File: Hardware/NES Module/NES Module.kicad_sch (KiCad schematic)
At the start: 3 parts, among them J1 Conn_01x31, J2 Conn_01x31, J3 Conn_02x36_Top_Bottom

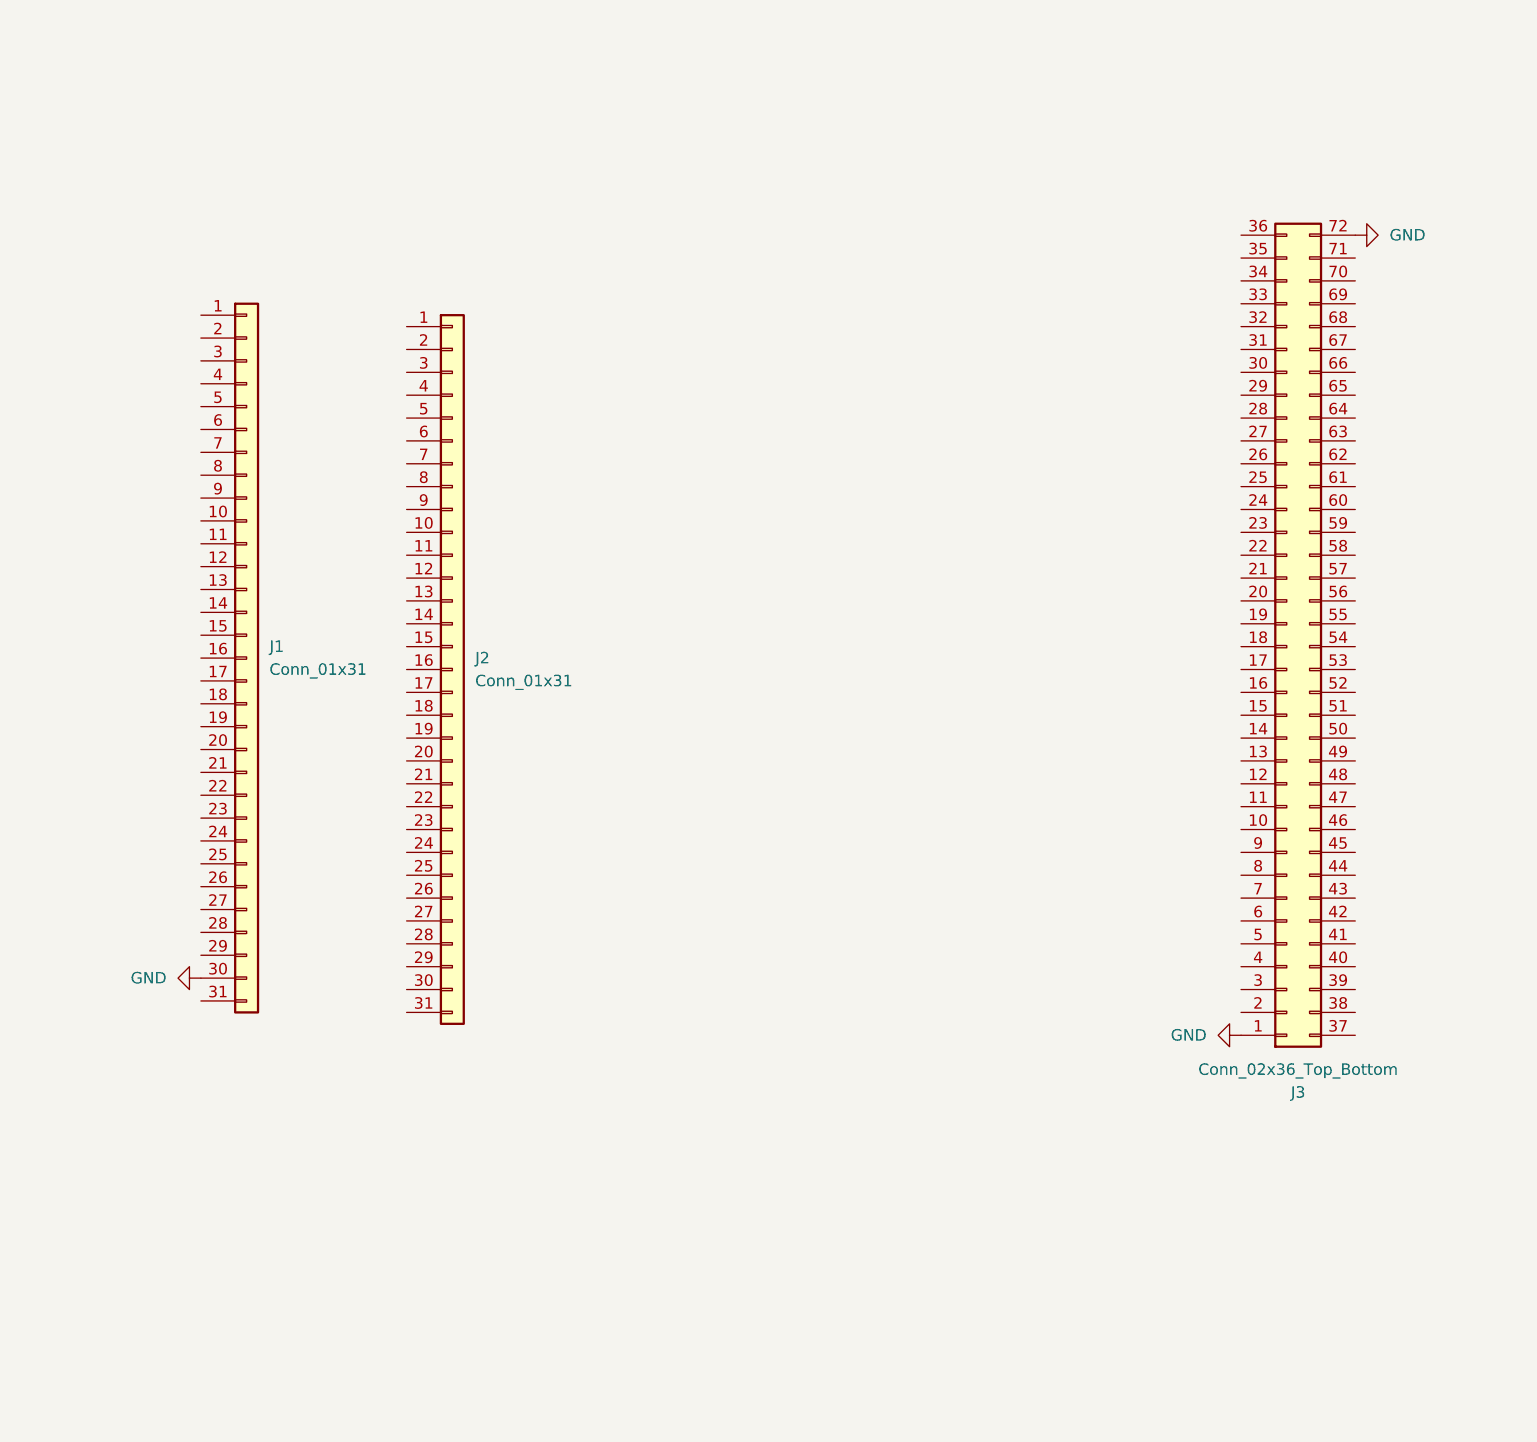
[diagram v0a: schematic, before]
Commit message: Created PCBs for more Cartridges, and fleshed out imagery in the PC Program
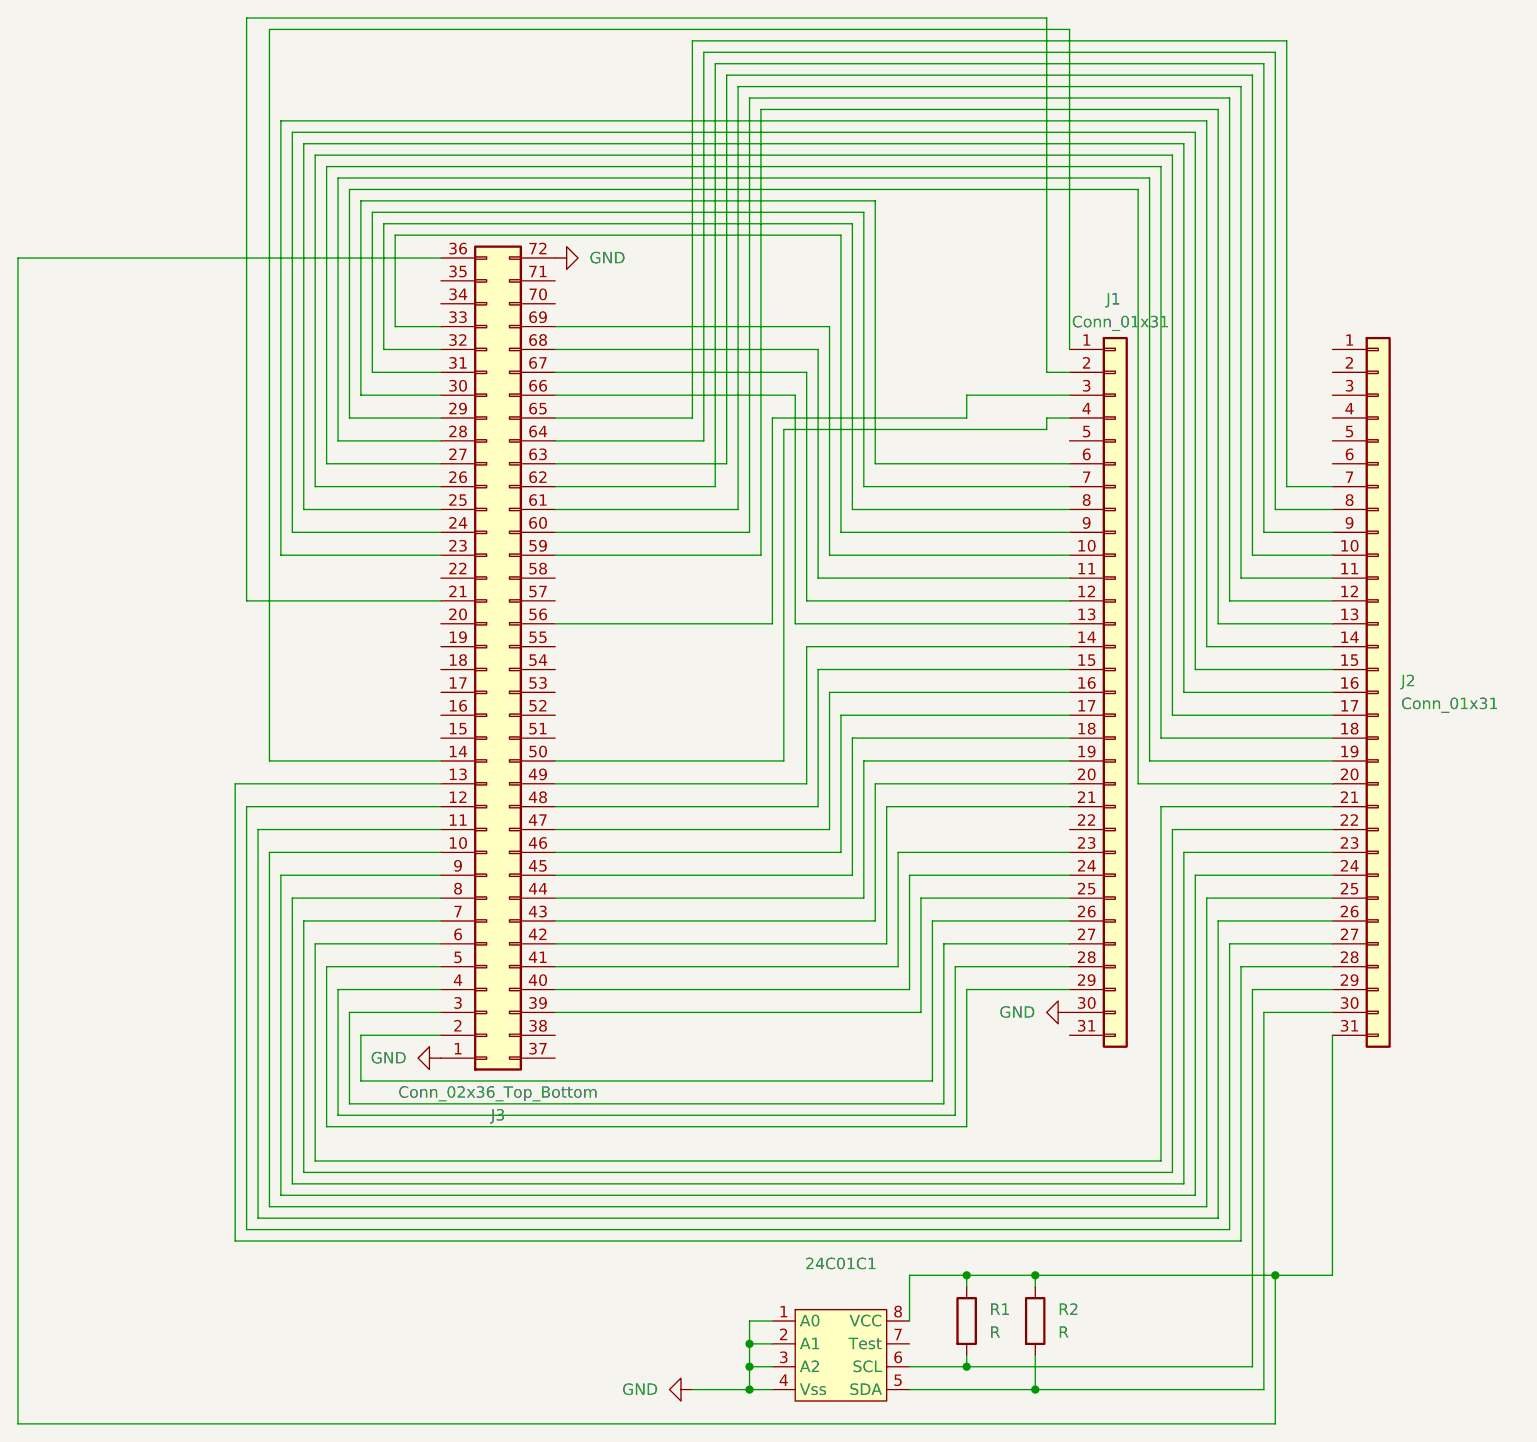
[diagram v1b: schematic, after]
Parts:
- added 24C01C1: ~, Package_DIP:DIP-8_W7.62mm, symbol SCARAB-Library:24C01C_-_!/P
- added R1, R2: R, Resistor_THT:R_Axial_DIN0207_L6.3mm_D2.5mm_P10.16mm_Horizontal, symbol Device:R
- J3: footprint (none) -> SCARAB:NES_Cartridge_Port
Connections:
- net GND: now also 24C01C1.1 (A0), 24C01C1.2 (A1), 24C01C1.3 (A2), 24C01C1.4 (Vss)
- net at J2.10 (Pin_10): now also J3.63 (Pin_63)
- net at J2.11 (Pin_11): now also J3.61 (Pin_61)
- net at J2.12 (Pin_12): now also J3.60 (Pin_60)
- net at J2.13 (Pin_13): now also J3.59 (Pin_59)
- net at J2.14 (Pin_14): now also J3.23 (Pin_23)
- net at J2.15 (Pin_15): now also J3.24 (Pin_24)
- net at J2.16 (Pin_16): now also J3.25 (Pin_25)
- net at J2.17 (Pin_17): now also J3.26 (Pin_26)
- net at J2.18 (Pin_18): now also J3.27 (Pin_27)
- net at J2.19 (Pin_19): now also J3.28 (Pin_28)
- net at J2.20 (Pin_20): now also J3.29 (Pin_29)
- net at J2.21 (Pin_21): now also J3.6 (Pin_6)
- net at J2.22 (Pin_22): now also J3.7 (Pin_7)
- net at J2.23 (Pin_23): now also J3.8 (Pin_8)
- net at J2.24 (Pin_24): now also J3.9 (Pin_9)
- net at J2.25 (Pin_25): now also J3.10 (Pin_10)
- net at J2.26 (Pin_26): now also J3.11 (Pin_11)
- net at J2.27 (Pin_27): now also J3.12 (Pin_12)
- net at J2.28 (Pin_28): now also J3.13 (Pin_13)
- net at J2.29 (Pin_29): now also 24C01C1.6 (SCL), R1.2
- net at J2.30 (Pin_30): now also 24C01C1.5 (SDA), R2.2
- net at J2.31 (Pin_31): now also J3.36 (Pin_36), 24C01C1.8 (VCC), R1.1, R2.1
- net at J2.7 (Pin_7): now also J3.65 (Pin_65)
- net at J2.8 (Pin_8): now also J3.64 (Pin_64)
- net at J2.9 (Pin_9): now also J3.62 (Pin_62)
- net at J3.14 (Pin_14): now also J1.1 (Pin_1)
- net at J3.2 (Pin_2): now also J1.26 (Pin_26)
- net at J3.21 (Pin_21): now also J1.2 (Pin_2)
- net at J3.3 (Pin_3): now also J1.27 (Pin_27)
- net at J3.30 (Pin_30): now also J1.6 (Pin_6)
- net at J3.31 (Pin_31): now also J1.7 (Pin_7)
- net at J3.32 (Pin_32): now also J1.8 (Pin_8)
- net at J3.33 (Pin_33): now also J1.9 (Pin_9)
- net at J3.39 (Pin_39): now also J1.25 (Pin_25)
- net at J3.4 (Pin_4): now also J1.28 (Pin_28)
- net at J3.40 (Pin_40): now also J1.24 (Pin_24)
- net at J3.41 (Pin_41): now also J1.23 (Pin_23)
- net at J3.42 (Pin_42): now also J1.21 (Pin_21)
- net at J3.43 (Pin_43): now also J1.20 (Pin_20)
- net at J3.44 (Pin_44): now also J1.19 (Pin_19)
- net at J3.45 (Pin_45): now also J1.18 (Pin_18)
- net at J3.46 (Pin_46): now also J1.17 (Pin_17)
- net at J3.47 (Pin_47): now also J1.16 (Pin_16)
- net at J3.48 (Pin_48): now also J1.15 (Pin_15)
- net at J3.49 (Pin_49): now also J1.14 (Pin_14)
- net at J3.5 (Pin_5): now also J1.29 (Pin_29)
- net at J3.50 (Pin_50): now also J1.4 (Pin_4)
- net at J3.56 (Pin_56): now also J1.3 (Pin_3)
- net at J3.66 (Pin_66): now also J1.13 (Pin_13)
- net at J3.67 (Pin_67): now also J1.12 (Pin_12)
- net at J3.68 (Pin_68): now also J1.11 (Pin_11)
- net at J3.69 (Pin_69): now also J1.10 (Pin_10)
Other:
- moved on the sheet: J1, J2, J3

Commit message: edited nes module board
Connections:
- net at J2.3 (Pin_3): now also J3.38 (Pin_38)
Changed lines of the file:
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@@
+	(wire
+		(pts
+			(xy 173.99 60.96) (xy 173.99 59.69)
+		)
+		(stroke
+			(width 0)
+			(type default)
+		)
+	)
 	(wire
 		(pts
@@
 	(wire
 		(pts
+			(xy 135.89 60.96) (xy 173.99 60.96)
+		)
+		(stroke
+			(width 0)
+			(type default)
+		)
+	)
+	(wire
+		(pts
 			(xy 133.35 125.73) (xy 133.35 140.97)
 		)
@@
 	(wire
 		(pts
+			(xy 135.89 130.81) (xy 135.89 60.96)
+		)
+		(stroke
+			(width 0)
+			(type default)
+		)
+	)
+	(wire
+		(pts
 			(xy 102.87 20.32) (xy 102.87 62.23)
 		)
@@
 		)
 		(stroke
+			(width 0)
+			(type default)
+		)
+	)
+	(wire
+		(pts
+			(xy 87.63 130.81) (xy 135.89 130.81)
+		)
+		(stroke
